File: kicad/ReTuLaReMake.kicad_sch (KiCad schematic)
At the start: 23 parts, among them J1 40 Pin DIP Header, U1 ATF1508AS-10AU100

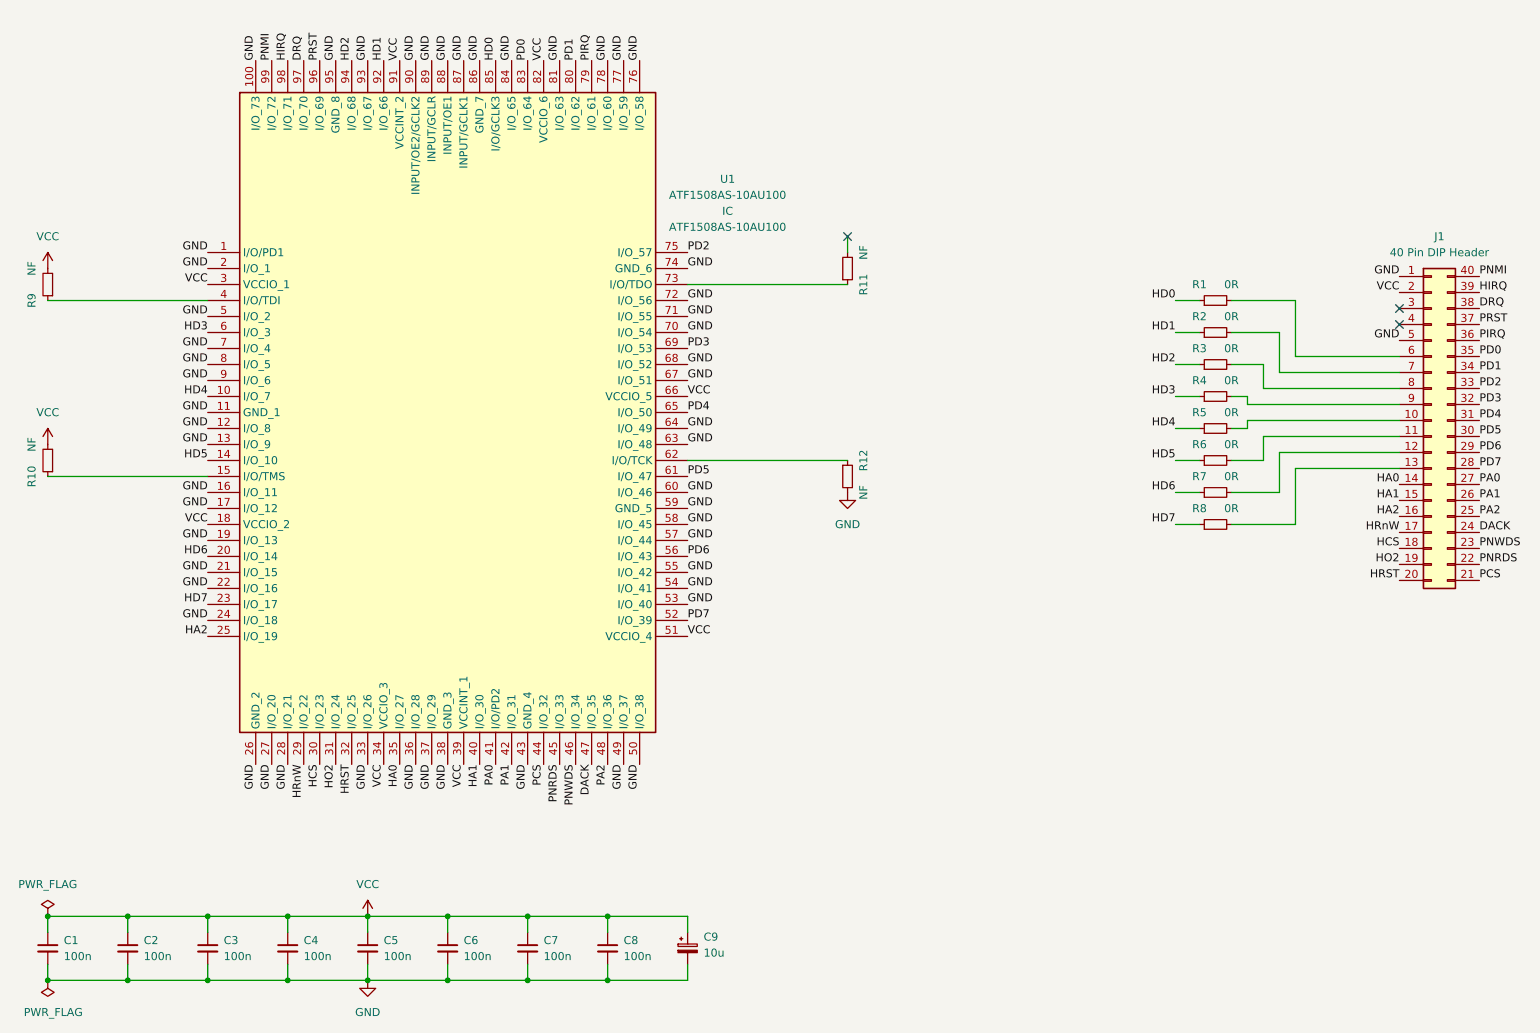
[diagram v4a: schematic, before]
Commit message: KiCAD: Rotated CPLD 180 degrees and changed pinout
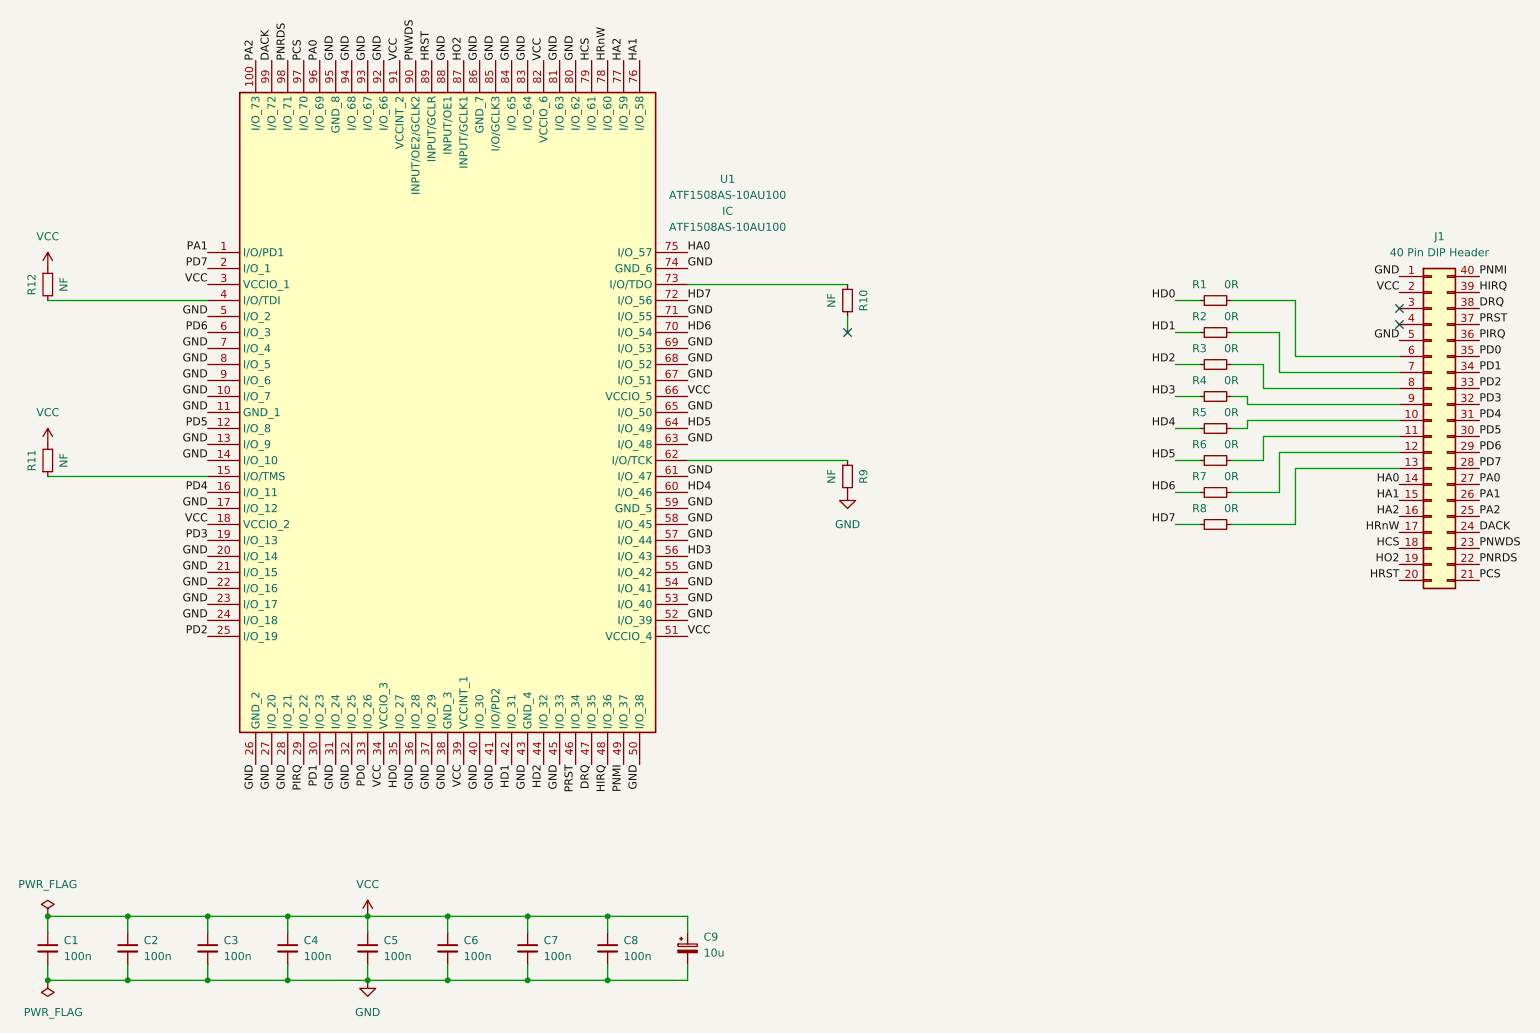
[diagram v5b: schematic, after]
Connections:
- net DACK: now also U1.99 (I/O_72); no longer U1.47 (I/O_35)
- net DRQ: now also U1.47 (I/O_35); no longer U1.97 (I/O_70)
- net GND: now also R9.2, U1.10 (I/O_7), U1.14 (I/O_10), U1.20 (I/O_14), U1.23 (I/O_17), U1.31 (I/O_24), U1.32 (I/O_25), U1.40 (I/O_30), U1.41 (I/O/PD2), U1.45 (I/O_33), U1.52 (I/O_39), U1.61 (I/O_47), U1.65 (I/O_50), U1.69 (I/O_53), U1.80 (I/O_62), U1.83 (I/O_64), U1.85 (I/O/GCLK3), U1.92 (I/O_66), U1.94 (I/O_68); no longer R12.2, U1.1 (I/O/PD1), U1.100 (I/O_73), U1.12 (I/O_8), U1.16 (I/O_11), U1.19 (I/O_13), U1.2 (I/O_1), U1.33 (I/O_26), U1.49 (I/O_37), U1.60 (I/O_46), U1.64 (I/O_49), U1.70 (I/O_54), U1.72 (I/O_56), U1.76 (I/O_58), U1.77 (I/O_59), U1.78 (I/O_60), U1.87 (INPUT/GCLK1), U1.89 (INPUT/GCLR), U1.90 (INPUT/OE2/GCLK2)
- net HA0: now also U1.75 (I/O_57); no longer U1.35 (I/O_27)
- net HA1: now also U1.76 (I/O_58); no longer U1.40 (I/O_30)
- net HA2: now also U1.77 (I/O_59); no longer U1.25 (I/O_19)
- net HCS: now also U1.79 (I/O_61); no longer U1.30 (I/O_23)
- net HD0: now also U1.35 (I/O_27); no longer U1.85 (I/O/GCLK3)
- net HD1: now also U1.42 (I/O_31); no longer U1.92 (I/O_66)
- net HD2: now also U1.44 (I/O_32); no longer U1.94 (I/O_68)
- net HD3: now also U1.56 (I/O_43); no longer U1.6 (I/O_3)
- net HD4: now also U1.60 (I/O_46); no longer U1.10 (I/O_7)
- net HD5: now also U1.64 (I/O_49); no longer U1.14 (I/O_10)
- net HD6: now also U1.70 (I/O_54); no longer U1.20 (I/O_14)
- net HD7: now also U1.72 (I/O_56); no longer U1.23 (I/O_17)
- net HIRQ: now also U1.48 (I/O_36); no longer U1.98 (I/O_71)
- net HO2: now also U1.87 (INPUT/GCLK1); no longer U1.31 (I/O_24)
- net HRST: now also U1.89 (INPUT/GCLR); no longer U1.32 (I/O_25)
- net HRnW: now also U1.78 (I/O_60); no longer U1.29 (I/O_22)
- net PA0: now also U1.96 (I/O_69); no longer U1.41 (I/O/PD2)
- net PA1: now also U1.1 (I/O/PD1); no longer U1.42 (I/O_31)
- net PA2: now also U1.100 (I/O_73); no longer U1.48 (I/O_36)
- net PCS: now also U1.97 (I/O_70); no longer U1.44 (I/O_32)
- net PD0: now also U1.33 (I/O_26); no longer U1.83 (I/O_64)
- net PD1: now also U1.30 (I/O_23); no longer U1.80 (I/O_62)
- net PD2: now also U1.25 (I/O_19); no longer U1.75 (I/O_57)
- net PD3: now also U1.19 (I/O_13); no longer U1.69 (I/O_53)
- net PD4: now also U1.16 (I/O_11); no longer U1.65 (I/O_50)
- net PD5: now also U1.12 (I/O_8); no longer U1.61 (I/O_47)
- net PD6: now also U1.6 (I/O_3); no longer U1.56 (I/O_43)
- net PD7: now also U1.2 (I/O_1); no longer U1.52 (I/O_39)
- net PIRQ: now also U1.29 (I/O_22); no longer U1.79 (I/O_61)
- net PNMI: now also U1.49 (I/O_37); no longer U1.99 (I/O_72)
- net PNRDS: now also U1.98 (I/O_71); no longer U1.45 (I/O_33)
- net PNWDS: now also U1.90 (INPUT/OE2/GCLK2); no longer U1.46 (I/O_34)
- net PRST: now also U1.46 (I/O_34); no longer U1.96 (I/O_69)
- net VCC: now also R11.2, R12.1; no longer R10.2, R9.2
- net at R10.1: now also U1.73 (I/O/TDO); no longer U1.15 (I/O/TMS)
- net at U1.4 (I/O/TDI): now also R12.2; no longer R9.1
- net at U1.62 (I/O/TCK): now also R9.1; no longer R12.1
- net at R11.1: now also U1.15 (I/O/TMS); no longer U1.73 (I/O/TDO)
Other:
- moved on the sheet: R10, R11, R12, R9

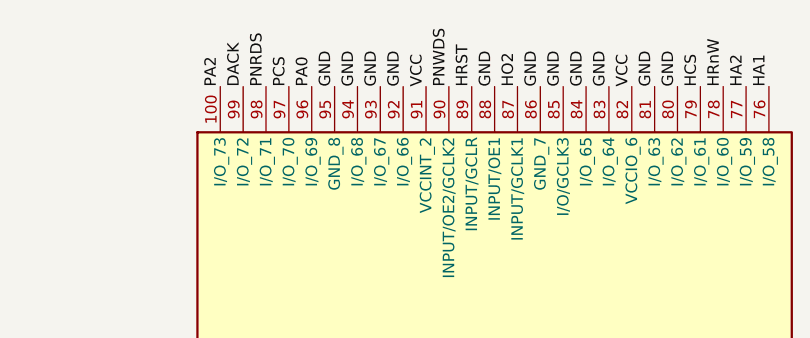
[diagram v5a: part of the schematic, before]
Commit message: KiCad: Move p_rd_b to a global clock
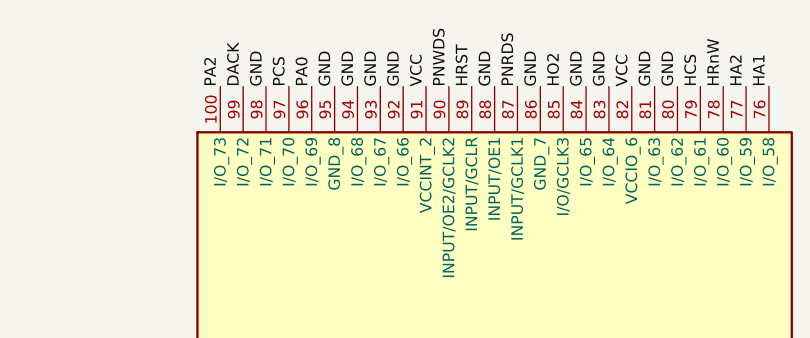
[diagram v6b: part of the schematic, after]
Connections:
- net GND: now also U1.98 (I/O_71); no longer U1.85 (I/O/GCLK3)
- net HO2: now also U1.85 (I/O/GCLK3); no longer U1.87 (INPUT/GCLK1)
- net PNRDS: now also U1.87 (INPUT/GCLK1); no longer U1.98 (I/O_71)
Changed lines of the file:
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@@
     (effects (font (size 1.27 1.27)) (justify left bottom))
   )
-  (label "PNRDS" (at 78.74 38.1 90)
+  (label "PNRDS" (at 106.68 38.1 90)
     (effects (font (size 1.27 1.27)) (justify left bottom))
   )
@@
     (effects (font (size 1.27 1.27)) (justify left bottom))
   )
-  (label "HO2" (at 106.68 38.1 90)
+  (label "HO2" (at 111.76 38.1 90)
     (effects (font (size 1.27 1.27)) (justify left bottom))
   )
@@
     (effects (font (size 1.27 1.27)) (justify left bottom))
   )
-  (label "GND" (at 111.76 38.1 90)
-    (effects (font (size 1.27 1.27)) (justify left bottom))
-  )
+  (label "GND" (at 78.74 38.1 90)
+    (effects (font (size 1.27 1.27)) (justify left bottom))
+  )
